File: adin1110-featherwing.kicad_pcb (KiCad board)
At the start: 4 copper layers, 50.8 x 22.9 mm, 25 parts, among them J1 4045_Connector_PH_2pos_RA_SMD, J2 4039_Header_Male_Vert_16pin_0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, J3 3096_USBC_RA_SMD, J4 4040_Header_Male_Vert_12pin_0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, Q1 4043_DMG3414_Nch_Mosfet_SOT23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, SW1 RST, U1 4042_MCP73831_Battery_Charger, U2 3093_MIC5225_3v3, U3 CRG, U4 STAT, U5 PWR

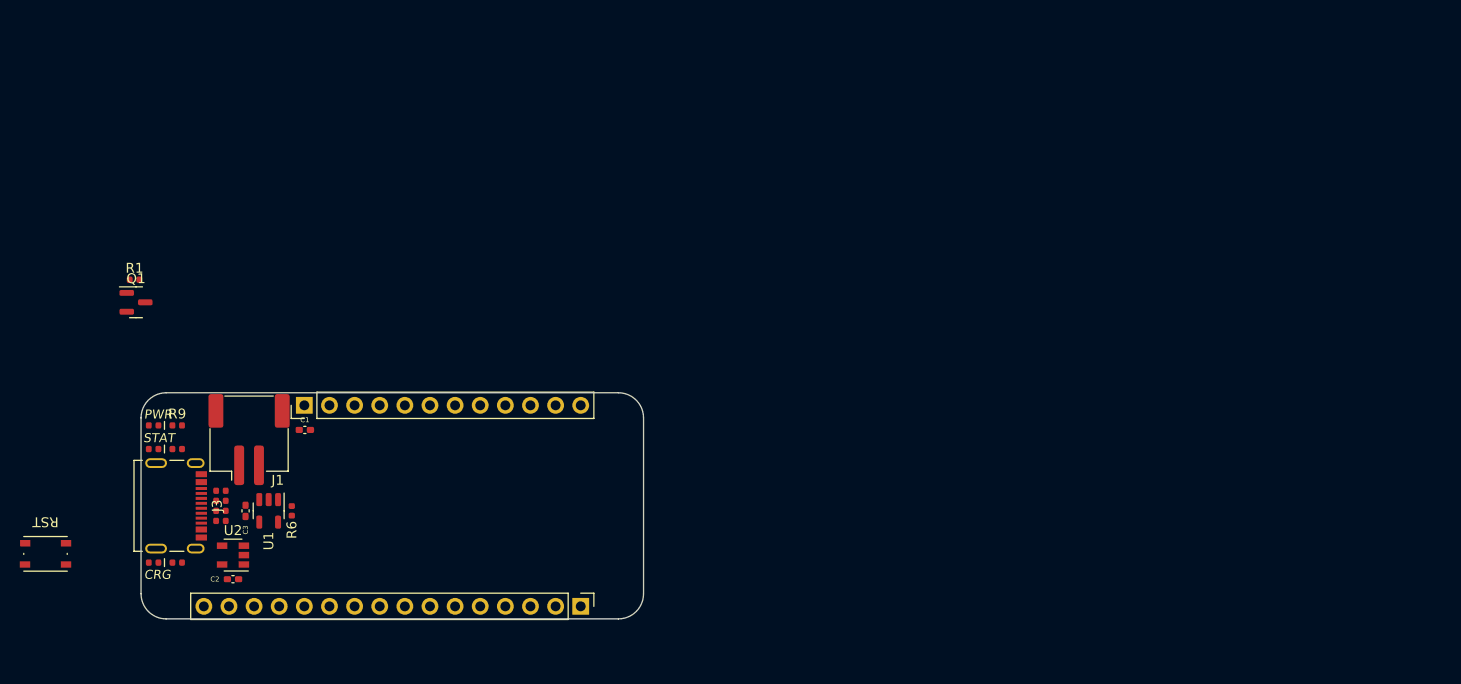
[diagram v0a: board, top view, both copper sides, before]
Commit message: sch almost done, started PCB placements
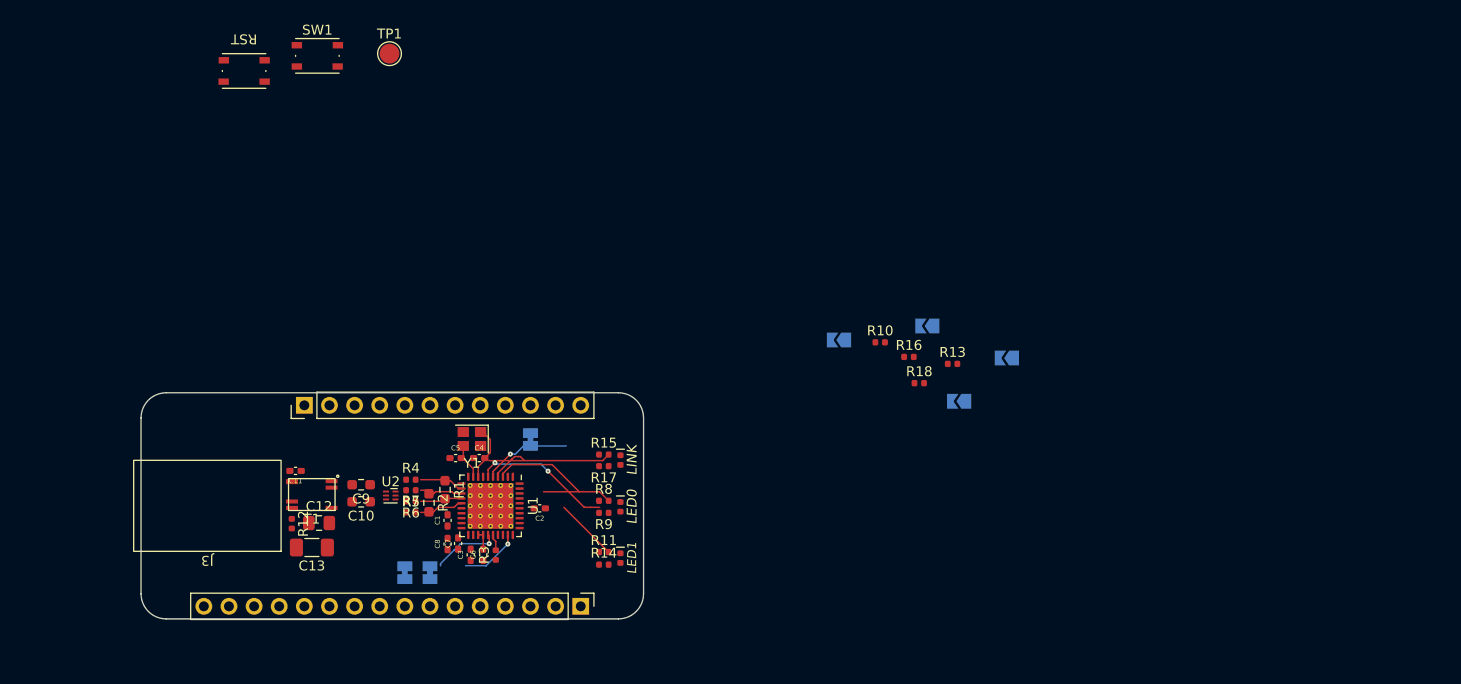
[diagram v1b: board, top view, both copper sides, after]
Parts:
- removed the J1 at (143.0, 86.6)
- removed Q1: 4043_DMG3414_Nch_Mosfet_SOT23-3, Shulltronics_Generics:SOT-23-3
- removed REF**: Shulltronics_Logo, Shulltronics_Generics:Shulltronics_Logo
- added C10: 4059_Cap_220nF_50V_0603, Resistor_SMD:R_0603_1608Metric_Pad0.98x0.95mm_HandSolder, F.Cu at (154.3, 92.3)
- added C11: 4063_Capacitor_100n_50V_0402, Shulltronics_Generics:C_0402_HandSolder, F.Cu at (147.7, 89.2)
- added C12: 4061_Capacitor_470nF_100V_0805, Capacitor_SMD:C_0805_2012Metric_Pad1.18x1.45mm_HandSolder, F.Cu at (150.1, 94.5)
- added C13: 4062_Capacitor_1nF_2kV_1206, Capacitor_SMD:C_1206_3216Metric_Pad1.33x1.80mm_HandSolder, F.Cu at (149.4, 96.9)
- added C4: 4055_Capacitor_10pF_50V_0402, Shulltronics_Generics:C_0402_HandSolder, F.Cu at (166.3, 87.9)
- added C5: 4055_Capacitor_10pF_50V_0402, Shulltronics_Generics:C_0402_HandSolder, F.Cu at (163.9, 87.9)
- added C6: 3089_Capacitor_100n_16V_0402, Shulltronics_Generics:C_0402_HandSolder, F.Cu at (166.7, 97.7)
- added C7: 4013_Capacitor_1u_16V_0402, Shulltronics_Generics:C_0402_HandSolder, F.Cu at (164.1, 96.5)
- added C8: 3089_Capacitor_100n_16V_0402, Shulltronics_Generics:C_0402_HandSolder, F.Cu at (163.1, 96.6)
- added C9: 4059_Cap_220nF_50V_0603, Resistor_SMD:R_0603_1608Metric_Pad0.98x0.95mm_HandSolder, F.Cu at (154.3, 90.6)
- added JP1: ~{INT}, Jumper:SolderJumper-2_P1.3mm_Bridged_Pad1.0x1.5mm, B.Cu at (158.8, 99.5)
- added JP2: ~{RST}, Jumper:SolderJumper-2_P1.3mm_Bridged_Pad1.0x1.5mm, B.Cu at (171.4, 86.0)
- added JP3: ~{CS}, Jumper:SolderJumper-2_P1.3mm_Bridged_Pad1.0x1.5mm, B.Cu at (161.3, 99.5)
- added JP4: ~{TX2P4_EN}, Jumper:SolderJumper-2_P1.3mm_Open_TrianglePad1.0x1.5mm, B.Cu at (202.6, 75.9)
- added JP5: SPI_CFG1, Jumper:SolderJumper-2_P1.3mm_Open_TrianglePad1.0x1.5mm, B.Cu at (219.6, 77.8)
- added JP6: ~{SWPD_EN}, Jumper:SolderJumper-2_P1.3mm_Open_TrianglePad1.0x1.5mm, B.Cu at (211.6, 74.5)
- added JP7: ~{MS_SEL}, Jumper:SolderJumper-2_P1.3mm_Open_TrianglePad1.0x1.5mm, B.Cu at (214.8, 82.1)
- added R10: 4064_Resistor_SMD_4k7_0.10W_1%, Shulltronics_Generics:RES-0402, F.Cu at (206.8, 76.2)
- added R11: 4064_Resistor_SMD_4k7_0.10W_1%, Shulltronics_Generics:RES-0402, F.Cu at (178.9, 97.4)
- added R12: 4038_Resistor_SMD_100_0.125W_1%, Shulltronics_Generics:RES-0402, F.Cu at (147.3, 94.5)
- added R13: 4064_Resistor_SMD_4k7_0.10W_1%, Shulltronics_Generics:RES-0402, F.Cu at (214.1, 78.4)
- added R15: 4064_Resistor_SMD_4k7_0.10W_1%, Shulltronics_Generics:RES-0402, F.Cu at (178.9, 87.5)
- added R16: 4064_Resistor_SMD_4k7_0.10W_1%, Shulltronics_Generics:RES-0402, F.Cu at (209.7, 77.7)
- added R17: 4038_Resistor_SMD_100_0.125W_1%, Shulltronics_Generics:RES-0402, F.Cu at (178.9, 88.7)
- added R18: 4064_Resistor_SMD_4k7_0.10W_1%, Shulltronics_Generics:RES-0402, F.Cu at (210.8, 80.3)
- added R9: 4038_Resistor_SMD_100_0.125W_1%, Shulltronics_Generics:RES-0402, F.Cu at (178.9, 93.4)
- added SW1: 4012_PushButton_NO_SMD, Shulltronics_ElectroMechanical:4012_PushButton_NO_SMD, F.Cu at (149.8, 47.1)
- added T1: 4057_Super_Tiny_Signal_Transformer, Shulltronics_Passives:4057_Super_Tiny_Signal_Transformer, F.Cu at (149.3, 91.6)
- added TP1: TestPoint, Shulltronics_Generics:TestPoint_Pad_D2.0mm, F.Cu at (157.2, 47.0)
- added Y1: 4056_Crystal_25MHz, Shulltronics_Passives:4004-Crystal-12MHz-4Pin_2.5x2.0mm, F.Cu at (165.5, 86.0)
- C1, C2, C3: value 4013_Capacitor_1u_16V_0402 -> 3089_Capacitor_100n_16V_0402
- J3: value 3096_USBC_RA_SMD -> 4060_TerminalBlock_NoScrew; footprint Shulltronics_Connectors:3096_USBC_RA -> Shulltronics_Connectors:4067_SPE_IP20
- R1: value 4017_Resistor_SMD_100k_0.125W_1%_1 -> 4066_Resistor_SMD_10k2_0.1W_1%_0603; footprint Shulltronics_Generics:RES-0402 -> Resistor_SMD:R_0603_1608Metric_Pad0.98x0.95mm_HandSolder
- R2: value 4011_Resistor_SMD_27_0.125W_1% -> 4066_Resistor_SMD_10k2_0.1W_1%_0603; footprint Shulltronics_Generics:RES-0402 -> Resistor_SMD:R_0603_1608Metric_Pad0.98x0.95mm_HandSolder
- R3: value 4011_Resistor_SMD_27_0.125W_1% -> 4065_Resistor_SMD_1k5_0.10W_1%
- R4: value 4009_Resistor_SMD_5k1_0.10W_1% -> 4053_Resistor_SMD_49.9_0.125W_1%
- R7: value 4038_Resistor_SMD_100_0.125W_1% -> 4053_Resistor_SMD_49.9_0.125W_1%
- R8: value 4038_Resistor_SMD_100_0.125W_1% -> 4064_Resistor_SMD_4k7_0.10W_1%
- U1: value 4042_MCP73831_Battery_Charger -> 4052_ADIN1110; footprint Shulltronics_Generics:SOT-23-5 -> Package_DFN_QFN:QFN-40-1EP_6x6mm_P0.5mm_EP4.6x4.6mm_ThermalVias
- U2: value 3093_MIC5225_3v3 -> 4058_TVS_2CH_Super_Speed; footprint Shulltronics_Regulators:3093_MIC5225_3v3_LDO -> Shulltronics_Integrated_Circuits:4058_TVS_2CH_Super_Speed
- U3: value CRG -> LED0
- U4: value STAT -> LED1
- U5: value PWR -> LINK
- moved SW2 52.8 mm to (142.6, 48.8)
- moved U4 48.5 mm to (180.5, 98.0), turned to 90 degrees
- moved U3 47.5 mm to (180.5, 92.8), turned to 90 degrees
- moved U5 47.3 mm to (180.5, 88.1), turned to 90 degrees
- moved R14 45.4 mm to (178.9, 98.7)
- moved R8 43.4 mm to (178.9, 92.2)
- moved R1 37.9 mm to (162.8, 91.1), turned to -90 degrees
- moved C2 31.8 mm to (172.4, 93.0)
- moved R3 28.3 mm to (167.9, 97.7), turned to 90 degrees
- moved R7 24.2 mm to (159.4, 93.4)
- moved C3 23.2 mm to (165.4, 97.7), turned to 90 degrees
- moved U1 22.4 mm to (167.4, 92.7)
- moved R2 21.0 mm to (161.2, 92.4), turned to -90 degrees
- moved R5 19.5 mm to (159.4, 91.1), turned to 180 degrees
- moved R4 19.2 mm to (159.4, 90.1)
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- renumbered J2 to J1, J4 to J2, R9 to R14, SW1 to SW2
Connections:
- C1 pad 2: VBAT -> VCC
- C3 pad 2: VDD -> VCC
- J1 pad 7: unconnected-(J2-Pad7) (its old number) -> /~{CS}_DEF
- J1 pad 8: unconnected-(J2-Pad8) (its old number) -> /~{INT}_DEF
- J2 pad 10: unconnected-(J4-Pad10) -> /~{RST}_DEF
- R1 pad 1: unconnected-(R1-Pad1) -> /TXN
- R1 pad 2: unconnected-(R1-Pad2) -> /RXP
- R14 pad 1: VCC -> Net-(R14-Pad1)
- R14 pad 2: Net-(R9-Pad2) -> VCC
- R2 pad 1: /D+ -> /RXN
- R2 pad 2: /USB_D+ -> /TXP
- R3 pad 1: /D- -> VCC
- R3 pad 2: /USB_D- -> /TEST1
- R4 pad 1: /CC1 -> Net-(R4-Pad1)
- R4 pad 2: GND -> /TXN
- R5 pad 1: /CC2 -> /RXN
- R5 pad 2: GND -> Net-(R4-Pad1)
- R6 pad 1: /PROG -> /RXP
- R6 pad 2: GND -> Net-(R6-Pad2)
- R7 pad 1: /STAT -> Net-(R6-Pad2)
- R7 pad 2: Net-(R7-Pad2) -> /TXP
- R8 pad 1: unconnected-(R8-Pad1) -> VCC
- R8 pad 2: Net-(R8-Pad2) -> /LED_0
- SW2 pad 1: GND -> unconnected-(SW2-Pad1)
- SW2 pad 2: /~{RST} -> unconnected-(SW2-Pad2)
- U1 pad 1: /STAT -> /MOSI
- U1 pad 2: GND -> /MISO
- U1 pad 3: VBAT -> /LED_0
- U1 pad 4: VDD -> /LINK_ST
- U1 pad 5: /PROG -> /~{RST}
- U2 pad 1: VDD -> Net-(C9-Pad1)
- U2 pad 2: GND -> Net-(C10-Pad1)
- U2 pad 3: /~{EN} -> GND
- U3 pad 1: VDD -> Net-(R9-Pad1)
- U3 pad 2: Net-(R7-Pad2) -> /LED_0
- U4 pad 1: Net-(R8-Pad2) -> Net-(R14-Pad1)
- U4 pad 2: GND -> /LED_1
- U5 pad 1: Net-(R9-Pad2) -> Net-(R17-Pad1)
- U5 pad 2: GND -> /LINK_ST
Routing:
- net /LED_1: track 0.00 -> 20.5 mm, vias 0 -> 2
- net /LED_0: track 0.00 -> 16.5 mm
- net /LINK_ST: track 0.00 -> 16.3 mm
- net /~{RST}: track 0.00 -> 9.00 mm, vias 0 -> 1
- net /~{INT}: track 0.00 -> 6.90 mm, vias 0 -> 1
- net /~{CS}: track 0.00 -> 6.10 mm, vias 0 -> 1
- net /XTAL_I: track 0.00 -> 5.56 mm
- net /TXP: track 0.00 -> 4.50 mm
- net /TXN: track 0.00 -> 4.49 mm
- net /RXN: track 0.00 -> 4.43 mm
- net /RXP: track 0.00 -> 4.24 mm
- net /XTAL_O: track 0.00 -> 3.79 mm
- net /1V1: track 0.00 -> 1.95 mm
- net /TEST1: track 0.00 -> 1.67 mm
- added copper zone on In1.Cu, net GND

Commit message: ready to order
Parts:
- removed G***: LOGO, Shulltronics_Generics:LOGO-feather
- removed SW1: 4012_PushButton_NO_SMD, Shulltronics_ElectroMechanical:4012_PushButton_NO_SMD
- added ?: , , F.Cu at (151.1, 84.9)
- added C14: 4069_Capacitor_3.3n_50V_0402, Shulltronics_Generics:C_0402_HandSolder, F.Cu at (145.9, 88.0)
- added J4: ~, Shulltronics_Connectors:4067_SPE_IP20, F.Cu at (135.9, 92.7)
- added L1: Shulltronics_Logo, Shulltronics_Generics:Shulltronics_Logo, F.Cu at (145.7, 85.6)
- added R19: 4065_Resistor_SMD_1k5_0.10W_1%, Shulltronics_Generics:RES-0402, F.Cu at (159.3, 97.1)
- added R20: 4064_Resistor_SMD_4k7_0.10W_1%, Shulltronics_Generics:RES-0402, F.Cu at (167.8, 97.2)
- added R21: 4008_Resistor_SMD_10k_0.125W_1%, Shulltronics_Generics:RES-0402, F.Cu at (176.1, 87.7)
- added REF**: SolderWirePad_1x01_SMD_1x2mm, Connector_Wire:SolderWirePad_1x01_SMD_1x2mm, B.Cu at (166.4, 84.9)
- added REF**: SolderWirePad_1x01_SMD_1x2mm, Connector_Wire:SolderWirePad_1x01_SMD_1x2mm, B.Cu at (156.2, 84.9)
- added REF**: SolderWirePad_1x01_SMD_1x2mm, Connector_Wire:SolderWirePad_1x01_SMD_1x2mm, B.Cu at (158.8, 84.9)
- added REF**: SolderWirePad_1x01_SMD_1x2mm, Connector_Wire:SolderWirePad_1x01_SMD_1x2mm, B.Cu at (168.9, 84.9)
- added REF**: SolderWirePad_1x01_SMD_1x2mm, Connector_Wire:SolderWirePad_1x01_SMD_1x2mm, B.Cu at (179.5, 102.8)
- added REF**: SolderWirePad_1x01_SMD_1x2mm, Connector_Wire:SolderWirePad_1x01_SMD_1x2mm, B.Cu at (156.2, 100.2)
- added REF**: SolderWirePad_1x01_SMD_1x2mm, Connector_Wire:SolderWirePad_1x01_SMD_1x2mm, B.Cu at (161.3, 84.9)
- added REF**: SolderWirePad_1x01_SMD_1x2mm, Connector_Wire:SolderWirePad_1x01_SMD_1x2mm, B.Cu at (148.6, 100.2)
- added REF**: SolderWirePad_1x01_SMD_1x2mm, Connector_Wire:SolderWirePad_1x01_SMD_1x2mm, B.Cu at (153.7, 100.3)
- added REF**: SolderWirePad_1x01_SMD_1x2mm, Connector_Wire:SolderWirePad_1x01_SMD_1x2mm, B.Cu at (163.8, 84.9)
- added REF**: SolderWirePad_1x01_SMD_1x2mm, Connector_Wire:SolderWirePad_1x01_SMD_1x2mm, B.Cu at (151.1, 100.2)
- added TP2: LED0, Shulltronics_Generics:TestPoint_Pad_D2.0mm, F.Cu at (185.6, 92.5)
- added TP3: LED1, Shulltronics_Generics:TestPoint_Pad_D2.0mm, F.Cu at (185.6, 97.6)
- added TP4: LINK, Shulltronics_Generics:TestPoint_Pad_D2.0mm, F.Cu at (185.5, 87.2)
- J3: footprint Shulltronics_Connectors:4067_SPE_IP20 -> TerminalBlock:TerminalBlock_bornier-2_P5.08mm
- R10, R13, R16, R18: moved to B.Cu
- TP1: value TestPoint -> 1V1
- U1: footprint Package_DFN_QFN:QFN-40-1EP_6x6mm_P0.5mm_EP4.6x4.6mm_ThermalVias -> Shulltronics_Integrated_Circuits:4052_ADIN1110_40QFN
- moved TP1 60.9 mm to (164.0, 107.5)
- moved SW2 51.4 mm to (136.8, 99.9)
- moved JP5 47.0 mm to (174.9, 92.2), turned to 0 degrees
- moved JP7 43.2 mm to (174.9, 98.9), turned to 0 degrees
- moved JP6 41.7 mm to (174.9, 94.4), turned to 0 degrees
- moved R13 39.5 mm to (177.1, 92.2), turned to -90 degrees
- moved R18 38.4 mm to (177.1, 98.9), turned to -90 degrees
- moved R16 36.6 mm to (177.1, 94.4), turned to -90 degrees
- moved R10 36.0 mm to (177.1, 96.7), turned to -90 degrees
- moved JP4 34.6 mm to (174.9, 96.7), turned to 0 degrees
- moved J3 3.71 mm to (136.1, 95.2), turned to 90 degrees
- moved C12 3.15 mm to (146.9, 94.7), turned to 180 degrees
- moved C2 2.41 mm to (170.1, 93.5), turned to 90 degrees
- moved R12 2.27 mm to (149.6, 94.7)
- moved C7 2.21 mm to (161.9, 96.5)
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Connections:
- net /RXN renamed /RX-
- net /RXP renamed /RX+
- net /TXN renamed /TX-
- net /TXP renamed /TX+
- net Net-(C10-Pad1) renamed /Db-
- net Net-(C10-Pad2) renamed /Da-
- net Net-(C9-Pad1) renamed /Db+
- net Net-(C9-Pad2) renamed /Da+
- J1 pad 1: unconnected-(J1-Pad1) -> /USER
- J1 pad 10: unconnected-(J1-Pad10) -> /A2
- J1 pad 11: unconnected-(J1-Pad11) -> /A1
- J1 pad 12: unconnected-(J1-Pad12) -> /A0
- J1 pad 9: unconnected-(J1-Pad9) -> /A3
- J2 pad 4: unconnected-(J2-Pad4) -> /D13
- J2 pad 5: unconnected-(J2-Pad5) -> /D12
- J2 pad 6: unconnected-(J2-Pad6) -> /D11
- J2 pad 7: unconnected-(J2-Pad7) -> /D10
- J2 pad 8: unconnected-(J2-Pad8) -> /D9
- J2 pad 9: unconnected-(J2-Pad9) -> /D6
- JP2 pad 1: /~{RST} -> /~{RESET}
- R4 pad 1: Net-(R4-Pad1) -> /Dc+
- R5 pad 2: Net-(R4-Pad1) -> /Dc+
- R6 pad 2: Net-(R6-Pad2) -> /Dc-
- R7 pad 1: Net-(R6-Pad2) -> /Dc-
- SW2 pad 1: unconnected-(SW2-Pad1) -> /~{RST}
- SW2 pad 2: unconnected-(SW2-Pad2) -> GND
- TP1 pad 1: unconnected-(TP1-Pad1) -> /1V1
- U1 pad 5: /~{RST} -> /~{RESET}
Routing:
- net Net-(C14-Pad2): track 0.00 -> 31.5 mm
- net VCC: track 0.00 -> 28.8 mm, vias 0 -> 11
- net /MISO: track 0.00 -> 19.5 mm, vias 0 -> 1
- net /MOSI: track 0.00 -> 17.8 mm, vias 0 -> 1
- net /SCK: track 0.00 -> 15.7 mm, vias 0 -> 1
- net /~{RESET}: track 0.00 -> 12.4 mm, vias 0 -> 2
- net /D-: track 0.00 -> 11.4 mm
- net /D+: track 0.00 -> 11.4 mm
- net /MS_SEL: track 0.00 -> 8.27 mm, vias 0 -> 1
- net /~{TX2P4_EN}: track 0.00 -> 6.60 mm, vias 0 -> 1
- net /SPI_CFG1: track 0.00 -> 6.45 mm, vias 0 -> 1
- net /~{SWPD_EN}: track 0.00 -> 6.39 mm, vias 0 -> 1
- net /~{INT}: track 6.90 -> 12.1 mm, vias 1 -> 2
- net Net-(T1-OUT1B): track 0.00 -> 3.91 mm
- net /~{CS}: track 6.10 -> 9.66 mm
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- added copper zone on B.Cu, net GND
- added copper zone on F.Cu, net VCC
- removed copper zone on In1.Cu, net GND
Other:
- board text added: "ADIN1110 FeatherWing"
- board text added: "rev A"

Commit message: as ordered for revA
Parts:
- removed the ? at (151.1, 84.9)
- removed the REF** at (166.4, 84.9)
- removed the REF** at (156.2, 84.9)
- removed the REF** at (158.8, 84.9)
- removed the REF** at (168.9, 84.9)
- removed the REF** at (179.5, 102.8)
- removed the REF** at (156.2, 100.2)
- removed the REF** at (161.3, 84.9)
- removed the REF** at (148.6, 100.2)
- removed the REF** at (153.7, 100.3)
- removed the REF** at (163.8, 84.9)
- removed the REF** at (151.1, 100.2)
- removed TP1: 1V1, Shulltronics_Generics:TestPoint_Pad_D2.0mm
- added ?: , , F.Cu at (158.8, 85.1)
- added ?: , , F.Cu at (156.2, 100.3)
- added ?: , , F.Cu at (148.6, 100.3)
- added ?: , , F.Cu at (166.4, 85.1)
- added ?: , , F.Cu at (168.9, 85.1)
- added ?: , , F.Cu at (153.7, 100.3)
- added ?: , , F.Cu at (163.8, 85.1)
- added ?: , , F.Cu at (156.2, 85.1)
- added ?: , , F.Cu at (161.3, 85.1)
- added ?: , , F.Cu at (151.1, 100.3)
- added REF**: TestPoint_Pad_2.0x2.0mm, TestPoint:TestPoint_Pad_2.0x2.0mm, B.Cu at (151.1, 85.1)
- TP2, TP3, TP4: footprint Shulltronics_Generics:TestPoint_Pad_D2.0mm -> Connector_Pin:Pin_D0.7mm_L6.5mm_W1.8mm_FlatFork; moved to B.Cu
- moved TP3 15.1 mm to (172.7, 89.8), turned to 180 degrees
- moved TP2 10.7 mm to (175.3, 89.8), turned to 180 degrees
- moved TP4 10.3 mm to (175.3, 85.8), turned to 180 degrees
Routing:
- net GND: track 2.42 -> 5.69 mm, vias 13 -> 12

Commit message: more rev 2 notes
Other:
- board text added: "REV 2 NOTES ( ) - add signal names on headers to top silkscreen"
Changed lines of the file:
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@@
   (gr_line (start 182.880001 101.600001) (end 182.88 83.82)
     (stroke (width 0.1) (type solid)) (layer "Edge.Cuts"))
+  (gr_text "REV 2 NOTES\n( ) - add signal names on headers to top silkscreen" (at 187.96 60.96) (layer "F.Cu")
+    (effects (font (size 1.524 1.524) (thickness 0.3048) bold) (justify left bottom))
+  )
   (gr_text "rev A" (at 141.2748 83.82) (layer "B.SilkS")
     (effects (font (size 1.016 1.016) (thickness 0.1524)) (justify left bottom mirror))
